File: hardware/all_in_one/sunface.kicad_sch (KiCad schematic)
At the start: 5 parts, among them U1 PT4115, U2 APH0630T330M

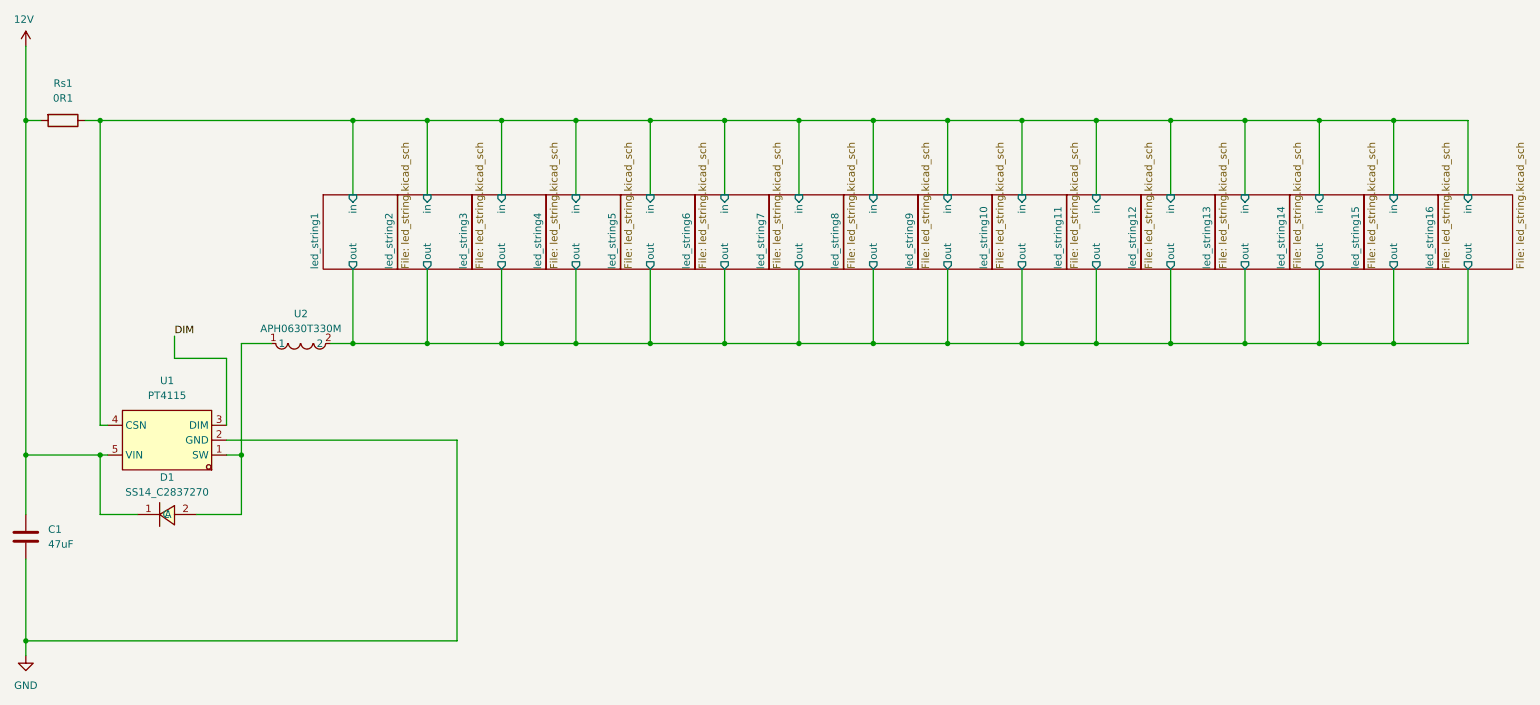
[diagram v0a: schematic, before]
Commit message: Added more leds
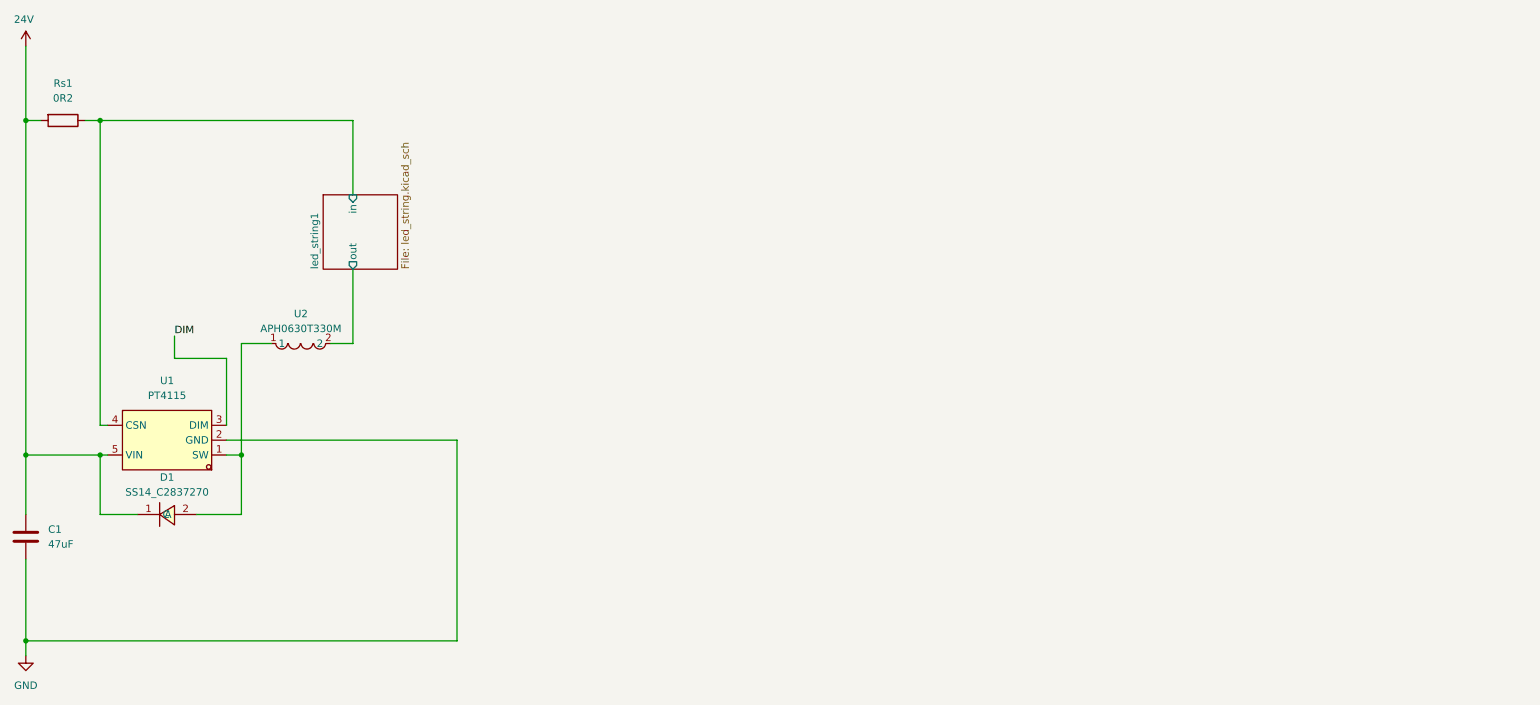
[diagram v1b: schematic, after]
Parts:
- Rs1: value 0R1 -> 0R2
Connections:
- net 12V renamed 24V
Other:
- removed sheet led_string10
- removed sheet led_string11
- removed sheet led_string12
- removed sheet led_string13
- removed sheet led_string14
- removed sheet led_string15
- removed sheet led_string16
- removed sheet led_string2
- removed sheet led_string3
- removed sheet led_string4
- removed sheet led_string5
- removed sheet led_string6
- removed sheet led_string7
- removed sheet led_string8
- removed sheet led_string9
